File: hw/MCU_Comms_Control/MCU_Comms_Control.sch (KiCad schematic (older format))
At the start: 32 parts, among them J1 USB_B_Mini, J2 CAN BUS, J3 TO_POWER_BOARD, J4 Mini-Debugging, J5 MULTI, SW1 BOOT, SW2 BUTTON, U1 SRV05-4, U2 SN65HVD230, U3 W25Q128JVS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

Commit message: advances were made on power electronics board
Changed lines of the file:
@@
 	0    -1   -1   0
 $EndComp
-Text GLabel 2000 4300 2    39   Input ~ 0
+Text GLabel 2000 4300 2    30   Input ~ 0
 ~ERROR
 $Comp

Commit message: remove old gerbers and assembly files
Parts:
- added J6: TEMP, Connector_PinHeader_2.54mm:PinHeader_2x02_P2.54mm_Vertical, symbol Connector:Conn_01x04_Male
- J1: footprint Connector_USB:USB_Micro-B_Molex-105017-0001 -> Connector_USB:USB_Micro-B_Molex-105133-0001
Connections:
- net +3V3: now also J6.3 (Pin_3)
- net GND: now also J6.4 (Pin_4)
- net NTC_PWR: now reaches U4.12 (PA2)
- net NTC_PWR: now also J3.7 (Pin_7)
- net at U4.40 (PB4): now also J6.1 (Pin_1)
- net at U4.41 (PB5): now also J6.2 (Pin_2)
- net USB_DM renamed USB_D-
- net USB_DP renamed USB_D+
- no-connect marks 10 -> 6
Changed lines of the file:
@@
 $EndDescr
-$Comp
-L MCU_ST_STM32F3:STM32F303CCTx U4
-U 1 1 5FB1FDE5
-P 4800 2750
-F 0 "U4" H 5050 1200 50  0000 C CNN
-F 1 "STM32F303CCTx" H 5300 1300 50  0000 C CNN
-F 2 "Package_QFP:LQFP-48_7x7mm_P0.5mm" H 4200 1350 50  0001 R CNN
-F 3 "http://www.st.com/st-web-ui/static/active/en/resource/technical/document/datasheet/DM00058181.pdf" H 4800 2750 50  0001 C CNN
-F 4 "C81523" H 4800 2750 50  0001 C CNN "LCSC"
-	1    4800 2750
-	1    0    0    -1
-$EndComp
 $Comp
 L power:+3V3 #PWR0101
@@
 CAN_TX
 Text GLabel 5400 3750 2    50   Input ~ 0
-USB_DP
+USB_D+
 Text GLabel 5400 3650 2    50   Input ~ 0
-USB_DM
+USB_D-
 $Comp
 L Device:R_Small R7
@@
 $EndComp
 Text GLabel 6300 3750 2    50   Input ~ 0
-USB_DP
+USB_D+
 Text GLabel 6100 3750 0    50   Input ~ 0
 SWDIO
@@
 F 0 "J1" H 957 7267 50  0000 C CNN
 F 1 "USB_B_Mini" H 957 7176 50  0000 C CNN
-F 2 "Connector_USB:USB_Micro-B_Molex-105017-0001" H 1050 6750 50  0001 C CNN
+F 2 "Connector_USB:USB_Micro-B_Molex-105133-0001" H 1050 6750 50  0001 C CNN
 F 3 "~" H 1050 6750 50  0001 C CNN
 	1    900  6800
@@
 HALL3
 NoConn ~ 1500 3700
-NoConn ~ 1500 3800
-Text Notes 1450 3800 2    50   ~ 10
+Text Notes 1450 3750 2    50   ~ 10
 RESERVED
 $Comp
@@
 $EndComp
 Text GLabel 1200 6900 2    50   Input ~ 0
-USB_DM
+USB_D-
 Text GLabel 1200 6800 2    50   Input ~ 0
-USB_DP
+USB_D+
 Text GLabel 2150 6800 0    50   Input ~ 0
-USB_DP
+USB_D+
 Text GLabel 2150 7000 0    50   Input ~ 0
-USB_DM
+USB_D-
 Wire Wire Line
 	2650 6400 1800 6400
@@
 Text Notes 5750 2850 0    50   ~ 0
 OPAMP3\n\nOPAMP1
-Text Notes 3400 2600 0    50   ~ 0
+Text Notes 3500 2650 0    50   ~ 0
 OPAMP2\n
 Text GLabel 4100 2750 0    50   Input ~ 0
@@
 Text GLabel 5400 2550 2    50   Input ~ 0
 BUTTON
-NoConn ~ 5400 2750
-NoConn ~ 4100 2950
-NoConn ~ 4100 3050
 NoConn ~ 1200 7000
 NoConn ~ 5250 7050
@@
 Connection ~ 3350 1800
 Text GLabel 3150 7000 2    50   Input ~ 0
-USB_DP
+USB_D+
 Text GLabel 3150 6800 2    50   Input ~ 0
-USB_DM
+USB_D-
 $Comp
 L Connector_Generic:Conn_02x13_Odd_Even J3
@@
 $EndComp
 NoConn ~ 5400 4050
+$Comp
+L MCU_ST_STM32F3:STM32F303CCTx U4
+U 1 1 5FB1FDE5
+P 4800 2750
+F 0 "U4" H 5050 1200 50  0000 C CNN
+F 1 "STM32F303CCTx" H 5300 1300 50  0000 C CNN
+F 2 "Package_QFP:LQFP-48_7x7mm_P0.5mm" H 4200 1350 50  0001 R CNN
+F 3 "http://www.st.com/st-web-ui/static/active/en/resource/technical/document/datasheet/DM00058181.pdf" H 4800 2750 50  0001 C CNN
+F 4 "C81523" H 4800 2750 50  0001 C CNN "LCSC"
+	1    4800 2750
+	1    0    0    -1
+$EndComp
+$Comp
+L power:GND #PWR01
+U 1 1 5FD220C9
+P 3400 3250
+F 0 "#PWR01" H 3400 3000 50  0001 C CNN
+F 1 "GND" H 3405 3077 50  0000 C CNN
+F 2 "" H 3400 3250 50  0001 C CNN
+F 3 "" H 3400 3250 50  0001 C CNN
+	1    3400 3250
+	1    0    0    -1
+$EndComp
+$Comp
+L Connector:Conn_01x04_Male J6
+U 1 1 5FD31C82
+P 3200 3050
+F 0 "J6" H 3308 3331 50  0000 C CNN
+F 1 "TEMP" H 3308 3240 50  0000 C CNN
+F 2 "Connector_PinHeader_2.54mm:PinHeader_2x02_P2.54mm_Vertical" H 3200 3050 50  0001 C CNN
+F 3 "~" H 3200 3050 50  0001 C CNN
+	1    3200 3050
+	1    0    0    -1
+$EndComp
+$Comp
+L power:+3.3V #PWR02
+U 1 1 5FD36362
+P 3400 3150
+F 0 "#PWR02" H 3400 3000 50  0001 C CNN
+F 1 "+3.3V" V 3415 3278 50  0000 L CNN
+F 2 "" H 3400 3150 50  0001 C CNN
+F 3 "" H 3400 3150 50  0001 C CNN
+	1    3400 3150
+	0    1    1    0
+$EndComp
+Wire Wire Line
+	3400 3050 4100 3050
+Wire Wire Line
+	4100 2950 3400 2950
+Text GLabel 1500 3800 0    50   Input ~ 0
+NTC_PWR
+Text GLabel 5400 2750 2    50   Input ~ 0
+NTC_PWR
 $EndSCHEMATC

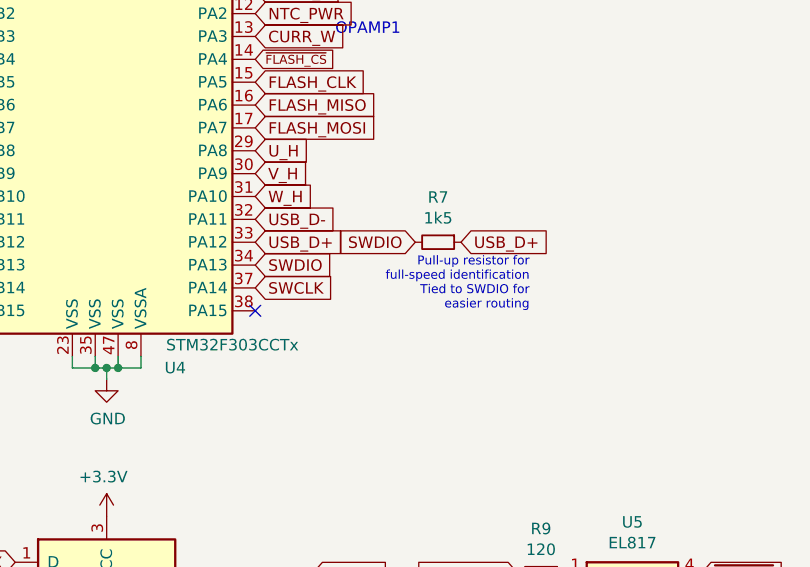
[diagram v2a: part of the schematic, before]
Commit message: new mcu board revision
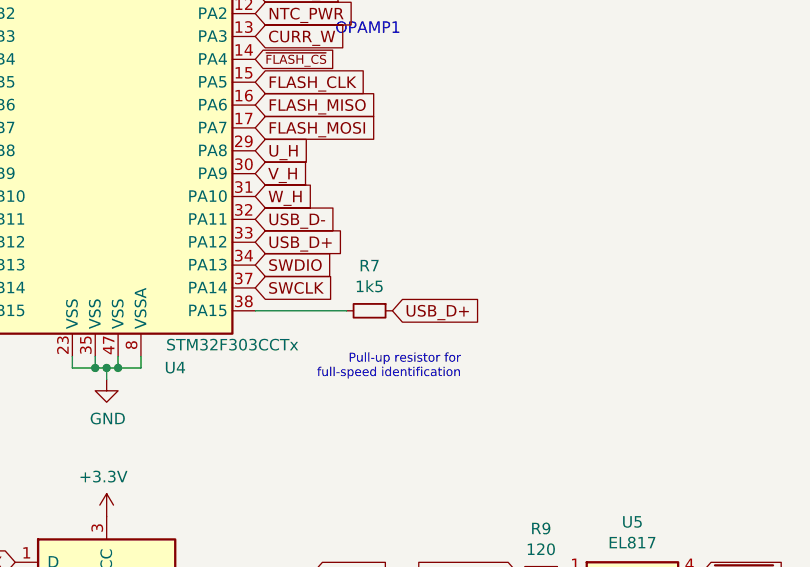
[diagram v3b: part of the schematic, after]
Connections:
- net SWDIO: no longer R7.2
- net at U4.38 (PA15): now also R7.2
- no-connect marks 6 -> 5
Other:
- note added: "Pull-up resistor for\nfull-speed identification"
- note removed: "Pull-up resistor for\nfull-speed identification\nTied to SWDIO for\neasier routing"
- moved on the sheet: R7
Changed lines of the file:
@@
 L Device:R_Small R7
 U 1 1 5FBA1869
-P 6200 3750
-F 0 "R7" V 6004 3750 50  0000 C CNN
-F 1 "1k5" V 6095 3750 50  0000 C CNN
-F 2 "Resistor_SMD:R_0603_1608Metric" H 6200 3750 50  0001 C CNN
-F 3 "~" H 6200 3750 50  0001 C CNN
-F 4 "C22843" H 6200 3750 50  0001 C CNN "LCSC"
-	1    6200 3750
+P 5900 4050
+F 0 "R7" V 5704 4050 50  0000 C CNN
+F 1 "1k5" V 5795 4050 50  0000 C CNN
+F 2 "Resistor_SMD:R_0603_1608Metric" H 5900 4050 50  0001 C CNN
+F 3 "~" H 5900 4050 50  0001 C CNN
+F 4 "C22843" H 5900 4050 50  0001 C CNN "LCSC"
+	1    5900 4050
 	0    1    1    0
 $EndComp
-Text GLabel 6300 3750 2    50   Input ~ 0
+Text GLabel 6000 4050 2    50   Input ~ 0
 USB_D+
-Text GLabel 6100 3750 0    50   Input ~ 0
-SWDIO
-Text Notes 6600 4050 2    39   ~ 0
-Pull-up resistor for\nfull-speed identification\nTied to SWDIO for\neasier routing
+Text Notes 6300 4350 2    39   ~ 0
+Pull-up resistor for\nfull-speed identification
 $Comp
 L Connector:USB_B_Mini J1
@@
 	1    0    0    -1
 $EndComp
-NoConn ~ 5400 4050
 $Comp
 L MCU_ST_STM32F3:STM32F303CCTx U4
@@
 Text GLabel 5400 2750 2    50   Input ~ 0
 NTC_PWR
+Wire Wire Line
+	5800 4050 5400 4050
 $EndSCHEMATC

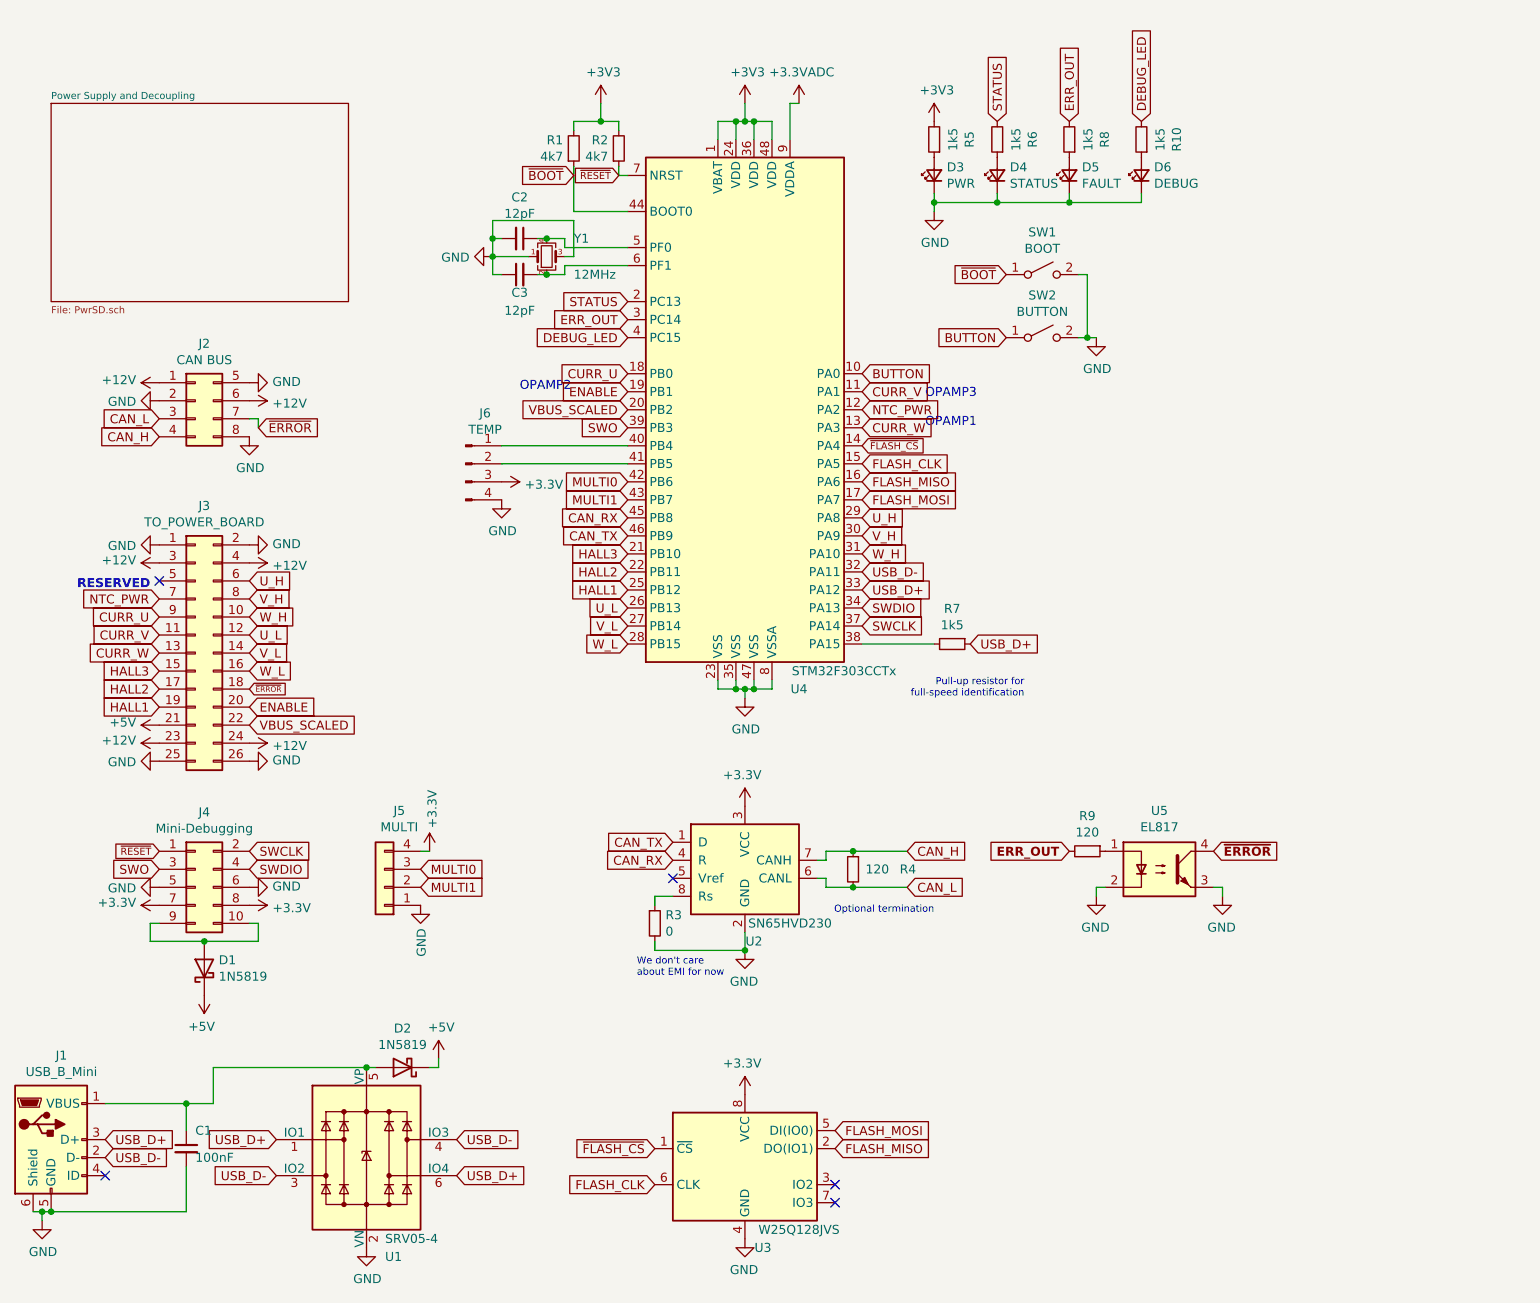
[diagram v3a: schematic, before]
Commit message: change stm32 to lfqp64 (schematic)
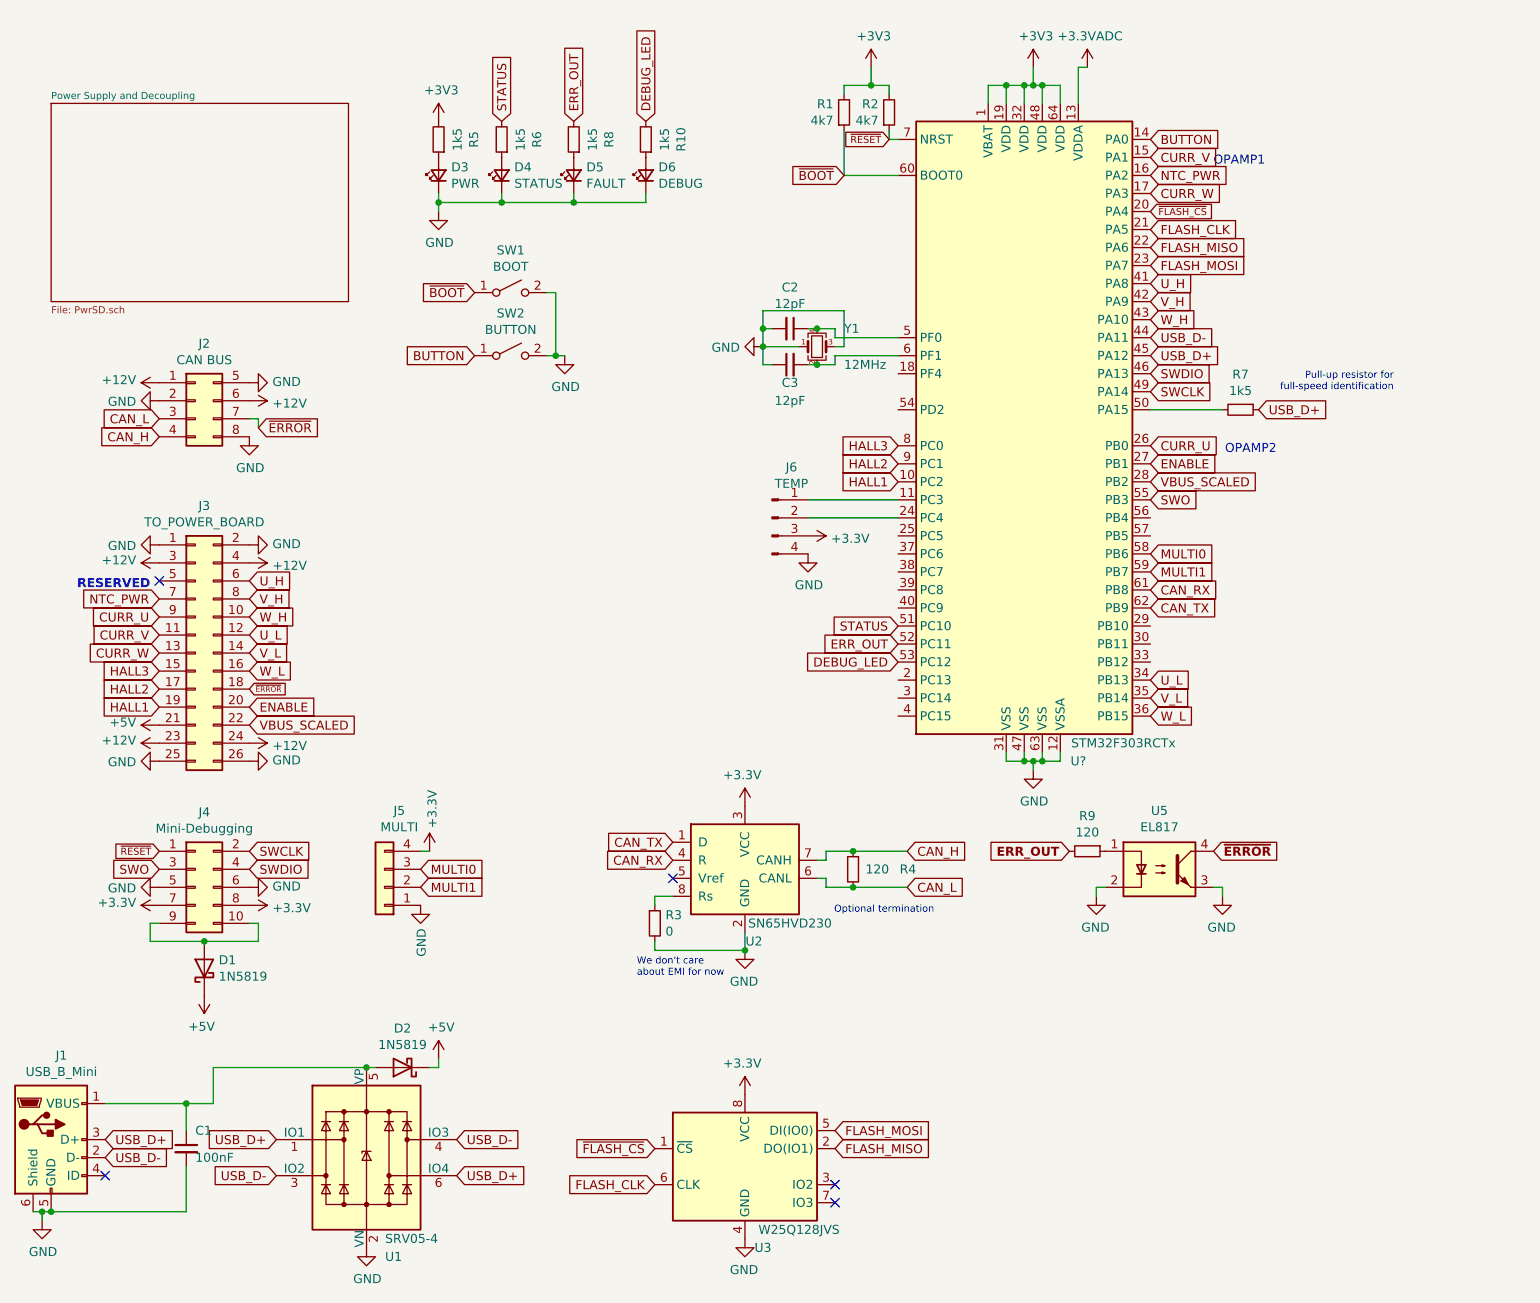
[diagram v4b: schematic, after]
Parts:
- removed U4: STM32F303CCTx, Package_QFP:LQFP-48_7x7mm_P0.5mm, symbol MCU_ST_STM32F3:STM32F303CCTx
- added U?: STM32F303RCTx, Package_QFP:LQFP-64_10x10mm_P0.5mm, symbol MCU_ST_STM32F3:STM32F303RCTx
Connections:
- net +3.3VADC: now also U?.13 (VDDA)
- net +3V3: now also U?.1 (VBAT), U?.19 (VDD), U?.32 (VDD), U?.48 (VDD), U?.64 (VDD)
- net BUTTON: now also U?.14 (PA0)
- net CAN_RX: now also U?.61 (PB8)
- net CAN_TX: now also U?.62 (PB9)
- net CURR_U: now also U?.26 (PB0)
- net CURR_V: now also U?.15 (PA1)
- net CURR_W: now also U?.17 (PA3)
- net DEBUG_LED: now also U?.53 (PC12)
- net ENABLE: now also U?.27 (PB1)
- net ERR_OUT: now also U?.52 (PC11)
- net FLASH_CLK: now also U?.21 (PA5)
- net FLASH_MISO: now also U?.22 (PA6)
- net FLASH_MOSI: now also U?.23 (PA7)
- net GND: now also U?.12 (VSSA), U?.31 (VSS), U?.47 (VSS), U?.63 (VSS)
- net HALL1: now also U?.10 (PC2)
- net HALL2: now also U?.9 (PC1)
- net HALL3: now also U?.8 (PC0)
- net MULTI0: now also U?.58 (PB6)
- net MULTI1: now also U?.59 (PB7)
- net NTC_PWR: now also U?.16 (PA2)
- net STATUS: now also U?.51 (PC10)
- net SWCLK: now also U?.49 (PA14)
- net SWDIO: now also U?.46 (PA13)
- net SWO: now also U?.55 (PB3)
- net USB_D+: now also U?.45 (PA12)
- net USB_D-: now also U?.44 (PA11)
- net U_H: now also U?.41 (PA8)
- net U_L: now also U?.34 (PB13)
- net VBUS_SCALED: now also U?.28 (PB2)
- net V_H: now also U?.42 (PA9)
- net V_L: now also U?.35 (PB14)
- net W_H: now also U?.43 (PA10)
- net W_L: now also U?.36 (PB15)
- net ~BOOT: now also U?.60 (BOOT0)
- net ~FLASH_CS: now also U?.20 (PA4)
- net ~RESET: now also U?.7 (NRST)
- net at R7.2: now also U?.50 (PA15)
- net at J6.1 (Pin_1): now also U?.11 (PC3)
- net at J6.2 (Pin_2): now also U?.24 (PC4)
- net at C2.1, Y1.4: now also U?.5 (PF0)
- net at C3.2, Y1.2: now also U?.6 (PF1)
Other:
- note added: "OPAMP1"
- note removed: "OPAMP3\n\nOPAMP1"
- moved on the sheet: C2, C3, D3, D4, D5, D6, J6, R1, R10, R2, R5, R6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
